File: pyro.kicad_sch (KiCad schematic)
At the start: 1 part, among them J2 Conn_01x03

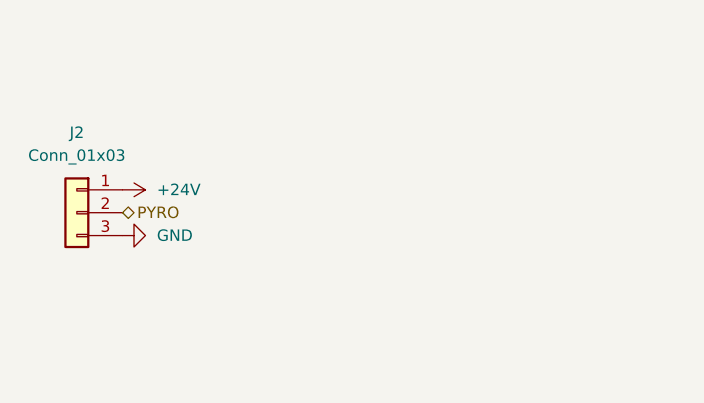
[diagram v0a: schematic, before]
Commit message: 24V Regulator, Pyro Igniter Circuit
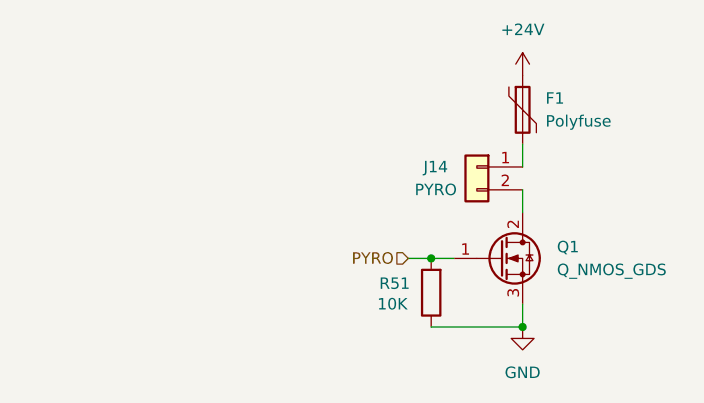
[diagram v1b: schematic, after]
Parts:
- removed J2: Conn_01x03, Connector_JST:JST_XH_B3B-XH-A_1x03_P2.50mm_Vertical, symbol Connector_Generic:Conn_01x03
- added F1: Polyfuse, symbol Device:Polyfuse
- added J14: PYRO, Connector_JST:JST_XH_B2B-XH-A_1x02_P2.50mm_Vertical, symbol Connector_Generic:Conn_01x02
- added Q1: Q_NMOS_GDS, symbol Transistor_FET:Q_NMOS_GDS
- added R51: 10K, Resistor_SMD:R_0402_1005Metric, symbol Device:R
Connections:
- net +24V: now also F1.1
- net GND: now also Q1.3 (S), R51.1
- net PYRO: now also Q1.1 (G), R51.2
- new net: F1.2, J14.1 (Pin_1)
- new net: J14.2 (Pin_2), Q1.2 (D)

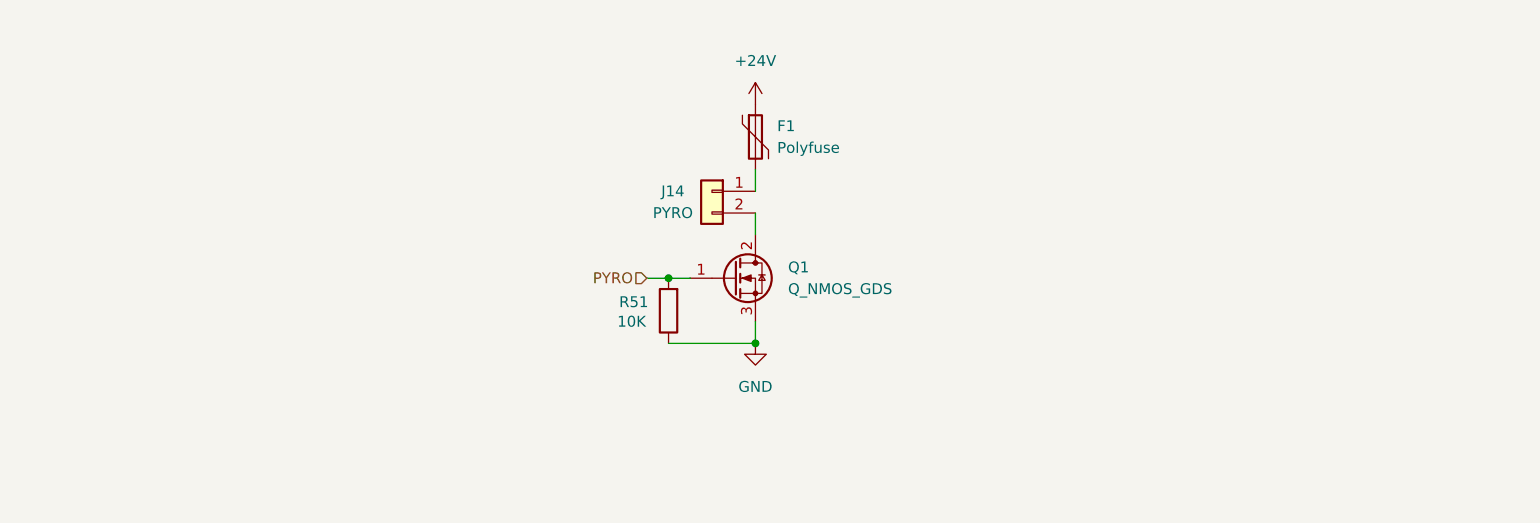
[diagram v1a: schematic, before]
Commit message: Pyro fault detection, Decoupling Caps STM32, Initial PCB Layout
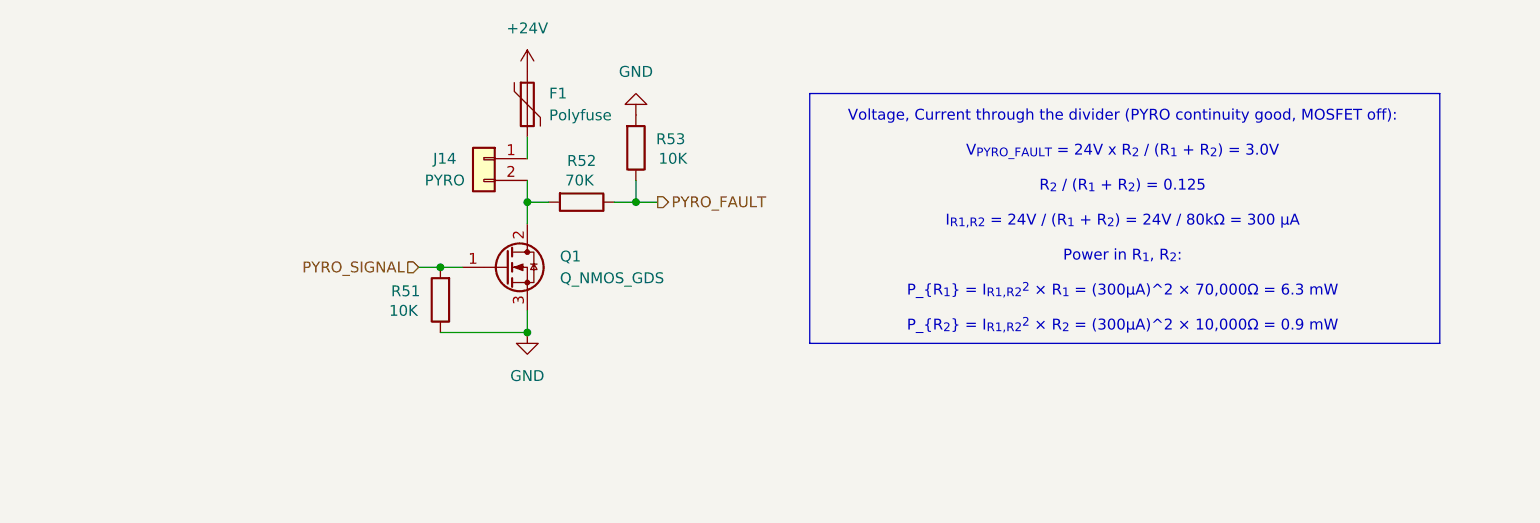
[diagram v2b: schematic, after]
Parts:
- added R52: 70K, Resistor_SMD:R_0402_1005Metric, symbol Device:R
- added R53: 10K, Resistor_SMD:R_0402_1005Metric, symbol Device:R
- F1: footprint (none) -> Fuse:Fuse_2920_7451Metric
- J14: footprint Connector_JST:JST_XH_B2B-XH-A_1x02_P2.50mm_Vertical -> Connector_JST:JST_XH_S2B-XH-A_1x02_P2.50mm_Horizontal
- Q1: footprint (none) -> Package_TO_SOT_SMD:TO-252-2
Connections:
- net GND: now also R53.2
- net at J14.2 (Pin_2), Q1.2 (D): now also R52.2
- net PYRO renamed PYRO_SIGNAL
- new net PYRO_FAULT: R52.1, R53.1
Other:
- note added: "Voltage, Current through the divider (PYRO continuity good, MOSFET off): V_{PYRO_FAULT} = 24V x R_{2} / (R_{1} + R_{2}) = 3.0V R_{2} / (R_{1} + R_{2}) = 0.125 I_{R1,R2} = 24V / (R_{1} + R_{2}) = 24V / 80kΩ = 300 µA Power in R_{1}, R_{2}: P_{R_{1}} = I_{R1,R2}^{2} × R_{1} = (300µA)^2 × 70,000Ω = 6.3 mW P_{R_{2}} = I_{R1,R2}^{2} × R_{2} = (300µA)^2 × 10,000Ω = 0.9 mW"
- moved on the sheet: F1, J14, Q1, R51

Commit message: Step files, SMD connectors, reduced size
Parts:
- removed Q1: Q_NMOS_GDS, Package_TO_SOT_SMD:TO-252-2, symbol Transistor_FET:Q_NMOS_GDS
- added Q1: CSD17571Q2, ElecSuper_ESN7414:ElecSuper_ESN7414, symbol Device:Q_NMOS
- F1: footprint Fuse:Fuse_2920_7451Metric -> Fuse:Fuse_1210_3225Metric
- J14: footprint Connector_JST:JST_XH_S2B-XH-A_1x02_P2.50mm_Horizontal -> Connector_JST:JST_PH_S2B-PH-SM4-TB_1x02-1MP_P2.00mm_Horizontal
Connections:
- net GND: now also Q1.S
- net PYRO_SIGNAL: now also Q1.G
- net at J14.2 (Pin_2), R52.2: now also Q1.D
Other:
- moved on the sheet: R51
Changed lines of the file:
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@@
+	)
+	(junction
+		(at 123.19 106.68)
+		(diameter 0)
+		(color 0 0 0 0)
+	)
+	(junction
+		(at 115.57 99.06)
+		(diameter 0)
+		(color 0 0 0 0)
 	)
 	(junction
@@
 	)
 	(junction
-		(at 113.03 99.06)
-		(diameter 0)
-		(color 0 0 0 0)
-	)
-	(junction
 		(at 123.19 91.44)
 		(diameter 0)
 		(color 0 0 0 0)
 	)
-	(junction
-		(at 123.19 106.68)
-		(diameter 0)
-		(color 0 0 0 0)
+	(wire
+		(pts
+			(xy 123.19 91.44) (xy 123.19 93.98)
+		)
+		(stroke
+			(width 0)
+			(type default)
+		)
 	)
 	(wire
@@
 	(wire
 		(pts
+			(xy 133.35 91.44) (xy 135.89 91.44)
+		)
+		(stroke
+			(width 0)
+			(type default)
+		)
+	)
+	(wire
+		(pts
 			(xy 123.19 104.14) (xy 123.19 106.68)
 		)
@@
 	(wire
 		(pts
-			(xy 123.19 93.98) (xy 123.19 91.44)
+			(xy 123.19 91.44) (xy 123.19 88.9)
+		)
+		(stroke
+			(width 0)
+			(type default)
+		)
+	)
+	(wire
+		(pts
+			(xy 123.19 83.82) (xy 123.19 86.36)
+		)
+		(stroke
+			(width 0)
+			(type default)
+		)
+	)
+	(wire
+		(pts
+			(xy 115.57 106.68) (xy 123.19 106.68)
+		)
+		(stroke
+			(width 0)
+			(type default)
+		)
+	)
+	(wire
+		(pts
+			(xy 135.89 91.44) (xy 138.43 91.44)
 		)
 		(stroke
@@
 		(pts
 			(xy 113.03 99.06) (xy 115.57 99.06)
-		)
-		(stroke
-			(width 0)
-			(type default)
-		)
-	)
-	(wire
-		(pts
-			(xy 133.35 91.44) (xy 135.89 91.44)
-		)
-		(stroke
-			(width 0)
-			(type default)
-		)
-	)
-	(wire
-		(pts
-			(xy 123.19 91.44) (xy 123.19 88.9)
-		)
-		(stroke
-			(width 0)
-			(type default)
-		)
-	)
-	(wire
-		(pts
-			(xy 123.19 83.82) (xy 123.19 86.36)
-		)
-		(stroke
-			(width 0)
-			(type default)
-		)
-	)
-	(wire
-		(pts
-			(xy 113.03 106.68) (xy 123.19 106.68)
-		)
-		(stroke
-			(width 0)
-			(type default)
-		)
-	)
-	(wire
-		(pts
-			(xy 135.89 91.44) (xy 138.43 91.44)
-		)
-		(stroke
-			(width 0)
-			(type default)
-		)
-	)
-	(wire
-		(pts
-			(xy 110.49 99.06) (xy 113.03 99.06)
 		)
 		(stroke
@@
 	(hierarchical_label "PYRO_SIGNAL"
 		(shape input)
-		(at 110.49 99.06 180)
+		(at 113.03 99.06 180)
 		(effects
 			(font
@@
 	(symbol
 		(lib_id "Device:R")
-		(at 113.03 102.87 180)
+		(at 115.57 102.87 180)
 		(unit 1)
 		(body_style 1)
@@
 		(dnp no)
 		(property "Reference" "R51"
-			(at 108.966 101.854 0)
+			(at 111.506 101.854 0)
 			(show_name no)
 			(do_not_autoplace no)
@@
 		)
 		(property "Value" "10K"
-			(at 108.712 104.14 0)
+			(at 111.252 104.14 0)
 			(show_name no)
 			(do_not_autoplace no)
@@
 		)
 		(property "Footprint" "Resistor_SMD:R_0402_1005Metric"
-			(at 114.808 102.87 90)
+			(at 117.348 102.87 90)
 			(hide yes)
 			(show_name no)
@@
 		)
 		(property "Datasheet" ""
-			(at 113.03 102.87 0)
+			(at 115.57 102.87 0)
 			(hide yes)
 			(show_name no)
@@
 		)
 		(property "Description" "Resistor"
-			(at 113.03 102.87 0)
+			(at 115.57 102.87 0)
 			(hide yes)
 			(show_name no)
@@
 			)
 		)
-		(property "Footprint" "Fuse:Fuse_2920_7451Metric"
+		(property "Footprint" "Fuse:Fuse_1210_3225Metric"
 			(at 124.46 85.09 0)
 			(hide yes)
@@
 				(path "/5c142d60-6b5a-463f-88b9-a177eae7f51b/d9a7688a-1f4c-4937-a470-cef945448846"
 					(reference "F3")
+					(unit 1)
+				)
+			)
+		)
+	)
+	(symbol
+		(lib_id "Device:Q_NMOS")
+		(at 120.65 99.06 0)
+		(unit 1)
+		(body_style 1)
+		(exclude_from_sim no)
+		(in_bom yes)
+		(on_board yes)
+		(in_pos_files yes)
+		(dnp no)
+		(fields_autoplaced yes)
+		(property "Reference" "Q1"
+			(at 127 97.7899 0)
+			(show_name no)
+			(do_not_autoplace no)
+			(effects
+				(font
+					(size 1.27 1.27)
+				)
+				(justify left)
+			)
+		)
+		(property "Value" "CSD17571Q2"
+			(at 127 100.3299 0)
+			(show_name no)
+			(do_not_autoplace no)
+			(effects
+				(font
+					(size 1.27 1.27)
+				)
+				(justify left)
+			)
+		)
+		(property "Footprint" "ElecSuper_ESN7414:ElecSuper_ESN7414"
+			(at 125.73 96.52 0)
+			(hide yes)
+			(show_name no)
+			(do_not_autoplace no)
+			(effects
+				(font
+					(size 1.27 1.27)
+				)
+			)
+		)
+		(property "Datasheet" "https://www.lcsc.com/datasheet/C962382.pdf?lcsc_vid=Q1JZU11RFQVYBlNfQVcMVVJQQwRZAwYFT1cPUgUDFQIxVlNeQFFXX1BUQFFXUjsOAxUeFF5JWBYZEEoKFBINSQcJGk4%3D"
+			(at 120.65 99.06 0)
+			(hide yes)
+			(show_name no)
+			(do_not_autoplace no)
+			(effects
+				(font
+					(size 1.27 1.27)
+				)
+			)
+		)
+		(property "Description" "N-Channel 30 V, 20 mΩ, SON 2×2 NexFET™ power TA = 25°C VALUE UNIT MOSFET i"
+			(at 120.65 99.06 0)
+			(hide yes)
+			(show_name no)
+			(do_not_autoplace no)
+			(effects
+				(font
+					(size 1.27 1.27)
+				)
+			)
+		)
+		(pin "G"
+		)
+		(pin "D"
+		)
+		(pin "S"
+		)
+		(instances
+			(project "mixed_signal_sensor_board"
+				(path "/5c142d60-6b5a-463f-88b9-a177eae7f51b/4774a8d6-944e-4a86-81b4-a8db3fe171f5"
+					(reference "Q4")
+					(unit 1)
+				)
+				(path "/5c142d60-6b5a-463f-88b9-a177eae7f51b/5edb0f01-38b3-4437-8c04-080f84fffaff"
+					(reference "Q1")
+					(unit 1)
+				)
+				(path "/5c142d60-6b5a-463f-88b9-a177eae7f51b/c1d5fa9f-2091-4637-b914-ef00b6553b9c"
+					(reference "Q2")
+					(unit 1)
+				)
+				(path "/5c142d60-6b5a-463f-88b9-a177eae7f51b/d9a7688a-1f4c-4937-a470-cef945448846"
+					(reference "Q3")
 					(unit 1)
 				)
@@
 	)
 	(symbol
-		(lib_id "Transistor_FET:Q_NMOS_GDS")
-		(at 120.65 99.06 0)
-		(unit 1)
-		(body_style 1)
-		(exclude_from_sim no)
-		(in_bom yes)
-		(on_board yes)
-		(in_pos_files yes)
-		(dnp no)
-		(fields_autoplaced yes)
-		(property "Reference" "Q1"
-			(at 127 97.7899 0)
-			(show_name no)
-			(do_not_autoplace no)
-			(effects
-				(font
-					(size 1.27 1.27)
-				)
-				(justify left)
-			)
-		)
-		(property "Value" "Q_NMOS_GDS"
-			(at 127 100.3299 0)
-			(show_name no)
-			(do_not_autoplace no)
-			(effects
-				(font
-					(size 1.27 1.27)
-				)
-				(justify left)
-			)
-		)
-		(property "Footprint" "Package_TO_SOT_SMD:TO-252-2"
-			(at 125.73 96.52 0)
-			(hide yes)
-			(show_name no)
-			(do_not_autoplace no)
-			(effects
-				(font
-					(size 1.27 1.27)
-				)
-			)
-		)
-		(property "Datasheet" ""
-			(at 120.65 99.06 0)
-			(hide yes)
-			(show_name no)
-			(do_not_autoplace no)
-			(effects
-				(font
-					(size 1.27 1.27)
-				)
-			)
-		)
-		(property "Description" "N-MOSFET transistor, gate/drain/source"
-			(at 120.65 99.06 0)
-			(hide yes)
-			(show_name no)
-			(do_not_autoplace no)
-			(effects
-				(font
-					(size 1.27 1.27)
-				)
-			)
-		)
-		(pin "3"
-		)
-		(pin "1"
-		)
-		(pin "2"
-		)
-		(instances
-			(project "mixed_signal_sensor_board"
-				(path "/5c142d60-6b5a-463f-88b9-a177eae7f51b/4774a8d6-944e-4a86-81b4-a8db3fe171f5"
-					(reference "Q4")
-					(unit 1)
-				)
-				(path "/5c142d60-6b5a-463f-88b9-a177eae7f51b/5edb0f01-38b3-4437-8c04-080f84fffaff"
-					(reference "Q1")
-					(unit 1)
-				)
-				(path "/5c142d60-6b5a-463f-88b9-a177eae7f51b/c1d5fa9f-2091-4637-b914-ef00b6553b9c"
-					(reference "Q2")
-					(unit 1)
-				)
-				(path "/5c142d60-6b5a-463f-88b9-a177eae7f51b/d9a7688a-1f4c-4937-a470-cef945448846"
-					(reference "Q3")
-					(unit 1)
-				)
-			)
-		)
-	)
-	(symbol
 		(lib_id "Connector_Generic:Conn_01x02")
 		(at 118.11 86.36 0)
@@
 			)
 		)
-		(property "Footprint" "Connector_JST:JST_XH_S2B-XH-A_1x02_P2.50mm_Horizontal"
+		(property "Footprint" "Connector_JST:JST_PH_S2B-PH-SM4-TB_1x02-1MP_P2.00mm_Horizontal"
 			(at 118.11 86.36 0)
 			(hide yes)

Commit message: Delvin protection, USB ESD protection, 02x06 pin socket
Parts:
- Q1: footprint ElecSuper_ESN7414:ElecSuper_ESN7414 -> CSD17571Q2:CSD17571Q2
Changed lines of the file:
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@@
 		(dnp no)
 		(fields_autoplaced yes)
-		(property "Reference" "#PWR0107"
+		(property "Reference" "#PWR0108"
 			(at 123.19 80.01 0)
 			(hide yes)
@@
 			(project "mixed_signal_sensor_board"
 				(path "/5c142d60-6b5a-463f-88b9-a177eae7f51b/4774a8d6-944e-4a86-81b4-a8db3fe171f5"
-					(reference "#PWR0116")
+					(reference "#PWR0117")
 					(unit 1)
 				)
 				(path "/5c142d60-6b5a-463f-88b9-a177eae7f51b/5edb0f01-38b3-4437-8c04-080f84fffaff"
-					(reference "#PWR0107")
+					(reference "#PWR0108")
 					(unit 1)
 				)
 				(path "/5c142d60-6b5a-463f-88b9-a177eae7f51b/c1d5fa9f-2091-4637-b914-ef00b6553b9c"
-					(reference "#PWR0110")
+					(reference "#PWR0111")
 					(unit 1)
 				)
 				(path "/5c142d60-6b5a-463f-88b9-a177eae7f51b/d9a7688a-1f4c-4937-a470-cef945448846"
-					(reference "#PWR0113")
+					(reference "#PWR0114")
 					(unit 1)
 				)
@@
 		(dnp no)
 		(fields_autoplaced yes)
-		(property "Reference" "#PWR0109"
+		(property "Reference" "#PWR0110"
 			(at 135.89 74.93 0)
 			(hide yes)
@@
 			(project "mixed_signal_sensor_board"
 				(path "/5c142d60-6b5a-463f-88b9-a177eae7f51b/4774a8d6-944e-4a86-81b4-a8db3fe171f5"
-					(reference "#PWR0118")
+					(reference "#PWR0119")
 					(unit 1)
 				)
 				(path "/5c142d60-6b5a-463f-88b9-a177eae7f51b/5edb0f01-38b3-4437-8c04-080f84fffaff"
-					(reference "#PWR0109")
+					(reference "#PWR0110")
 					(unit 1)
 				)
 				(path "/5c142d60-6b5a-463f-88b9-a177eae7f51b/c1d5fa9f-2091-4637-b914-ef00b6553b9c"
-					(reference "#PWR0112")
+					(reference "#PWR0113")
 					(unit 1)
 				)
 				(path "/5c142d60-6b5a-463f-88b9-a177eae7f51b/d9a7688a-1f4c-4937-a470-cef945448846"
-					(reference "#PWR0115")
+					(reference "#PWR0116")
 					(unit 1)
 				)
@@
 			)
 		)
-		(property "Footprint" "ElecSuper_ESN7414:ElecSuper_ESN7414"
+		(property "Footprint" "CSD17571Q2:CSD17571Q2"
 			(at 125.73 96.52 0)
 			(hide yes)
@@
 		(dnp no)
 		(fields_autoplaced yes)
-		(property "Reference" "#PWR0108"
+		(property "Reference" "#PWR0109"
 			(at 123.19 113.03 0)
 			(hide yes)
@@
 			(project "mixed_signal_sensor_board"
 				(path "/5c142d60-6b5a-463f-88b9-a177eae7f51b/4774a8d6-944e-4a86-81b4-a8db3fe171f5"
-					(reference "#PWR0117")
+					(reference "#PWR0118")
 					(unit 1)
 				)
 				(path "/5c142d60-6b5a-463f-88b9-a177eae7f51b/5edb0f01-38b3-4437-8c04-080f84fffaff"
-					(reference "#PWR0108")
+					(reference "#PWR0109")
 					(unit 1)
 				)
 				(path "/5c142d60-6b5a-463f-88b9-a177eae7f51b/c1d5fa9f-2091-4637-b914-ef00b6553b9c"
-					(reference "#PWR0111")
+					(reference "#PWR0112")
 					(unit 1)
 				)
 				(path "/5c142d60-6b5a-463f-88b9-a177eae7f51b/d9a7688a-1f4c-4937-a470-cef945448846"
-					(reference "#PWR0114")
-					(unit 1)
-				)
+					(reference "#PWR0115")
+					(unit 1)
+				)
